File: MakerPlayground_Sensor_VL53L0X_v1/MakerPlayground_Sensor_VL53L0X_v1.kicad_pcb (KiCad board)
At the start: 2 copper layers, 30.4 x 19.9 mm, 18 parts, among them J1 Connector, Q1 BSS138, Q2 BSS138, U1 VL53L0X, U2 AP2127K-3.3

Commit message: Complete design.
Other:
- board text added: "v1.0"
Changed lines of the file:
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@@
   (general
     (thickness 1.6)
-    (drawings 223)
+    (drawings 224)
     (tracks 143)
     (zones 0)
@@
     (pad 1 np_thru_hole circle (at 0 0) (size 3 3) (drill 3) (layers *.Cu *.Mask))
   )
+  (gr_text v1.0 (at 143.75 114) (layer F.SilkS)
+    (effects (font (size 0.5 0.5) (thickness 0.1)))
+  )
   (gr_line (start 147.105 114.758) (end 147.177 114.714) (layer Edge.Cuts) (width 0.1))

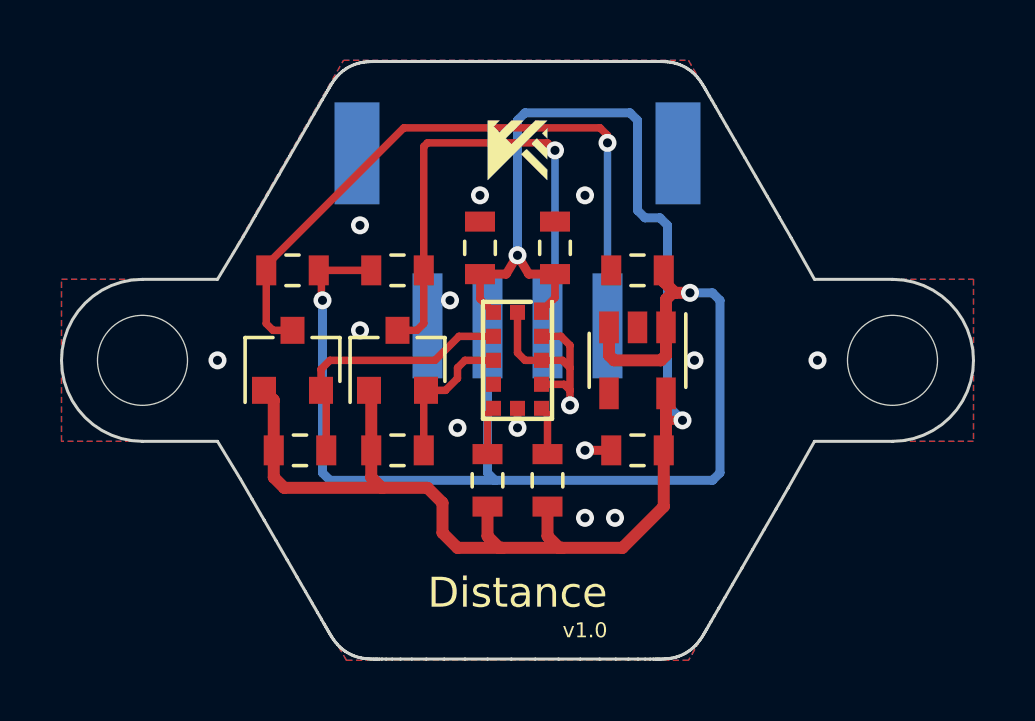
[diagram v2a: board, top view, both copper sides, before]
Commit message: Improve GND PTH, GND spreading area. Ready to fab.
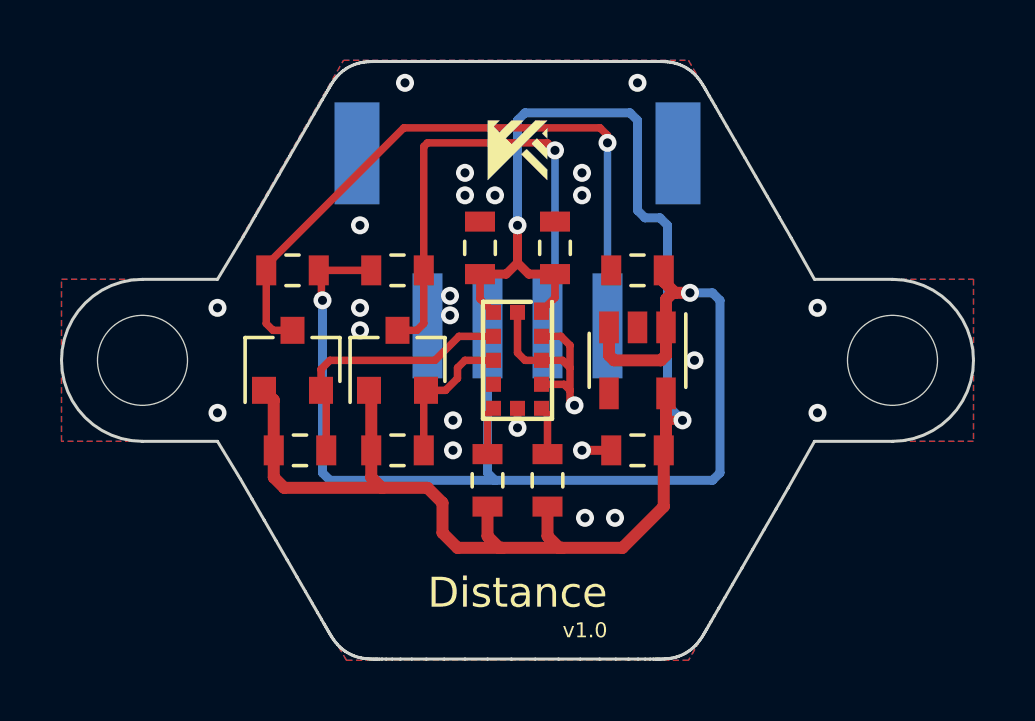
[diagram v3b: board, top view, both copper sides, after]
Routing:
- net GND: vias 14 -> 24
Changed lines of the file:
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@@
     (thickness 1.6)
     (drawings 224)
-    (tracks 143)
+    (tracks 154)
     (zones 0)
     (modules 18)
@@
     (44 Edge.Cuts user)
     (45 Margin user)
-    (46 B.CrtYd user)
-    (47 F.CrtYd user)
-    (48 B.Fab user)
-    (49 F.Fab user)
+    (46 B.CrtYd user hide)
+    (47 F.CrtYd user hide)
+    (48 B.Fab user hide)
+    (49 F.Fab user hide)
   )
   (setup
-    (last_trace_width 0.25)
+    (last_trace_width 0.3)
     (user_trace_width 0.15)
     (user_trace_width 0.2)
@@
     (fp_line (start -3.5 1.6) (end -3 0.892893) (layer B.Fab) (width 0.1))
     (fp_line (start -3 0.892893) (end -2.5 1.6) (layer B.Fab) (width 0.1))
-    (fp_text user %R (at 0 -1.5) (layer B.Fab)
+    (fp_text user %R (at 0 -1.5) (layer B.Fab) hide
       (effects (font (size 1 1) (thickness 0.15)) (justify mirror))
     )
@@
     (effects (font (size 1 1) (thickness 0.2)))
   )
-  (via (at 140.25 99.5) (size 0.6) (drill 0.3) (layers F.Cu B.Cu) (net 1))
-  (via (at 139.5 107.25) (size 0.6) (drill 0.3) (layers F.Cu B.Cu) (net 1))
-  (via (at 139.25 103) (size 0.6) (drill 0.3) (layers F.Cu B.Cu) (net 1))
+  (via (at 140.75 99.5) (size 0.6) (drill 0.3) (layers F.Cu B.Cu) (net 1))
+  (via (at 139.35 107) (size 0.6) (drill 0.3) (layers F.Cu B.Cu) (net 1))
+  (via (at 139.25 102.85) (size 0.6) (drill 0.3) (layers F.Cu B.Cu) (net 1))
   (segment (start 141.5 106.6) (end 141.5 107.25) (width 0.25) (layer F.Cu) (net 1))
   (via (at 141.5 107.25) (size 0.6) (drill 0.3) (layers F.Cu B.Cu) (net 1))
-  (via (at 143.75 108) (size 0.6) (drill 0.3) (layers F.Cu B.Cu) (net 1))
+  (via (at 143.65 108) (size 0.6) (drill 0.3) (layers F.Cu B.Cu) (net 1))
   (segment (start 144.5375 108) (end 143.75 108) (width 0.3) (layer F.Cu) (net 1) (status 10))
-  (via (at 131.5 105) (size 0.6) (drill 0.3) (layers F.Cu B.Cu) (net 1))
+  (via (at 131.5 106.75) (size 0.6) (drill 0.3) (layers F.Cu B.Cu) (net 1))
   (via (at 147.4 105) (size 0.6) (drill 0.3) (layers F.Cu B.Cu) (net 1))
   (segment (start 141.5 103.4) (end 141.5 104.75) (width 0.25) (layer F.Cu) (net 1))
   (segment (start 141.5 104.75) (end 141.75 105) (width 0.25) (layer F.Cu) (net 1))
   (segment (start 141.75 105) (end 142.3 105) (width 0.25) (layer F.Cu) (net 1))
-  (via (at 143.25 106.5) (size 0.6) (drill 0.3) (layers F.Cu B.Cu) (net 1))
+  (via (at 143.4 106.5) (size 0.6) (drill 0.3) (layers F.Cu B.Cu) (net 1))
   (segment (start 142.95 104.2) (end 143.25 104.5) (width 0.25) (layer F.Cu) (net 1))
   (segment (start 142.3 104.2) (end 142.95 104.2) (width 0.25) (layer F.Cu) (net 1))
@@
   (segment (start 143.25 105.25) (end 143.25 106) (width 0.25) (layer F.Cu) (net 1))
   (segment (start 143.25 106) (end 143.25 106.5) (width 0.25) (layer F.Cu) (net 1))
-  (via (at 143.75 99.5) (size 0.6) (drill 0.3) (layers F.Cu B.Cu) (net 1))
+  (via (at 143.65 99.5) (size 0.6) (drill 0.3) (layers F.Cu B.Cu) (net 1))
   (via (at 143.75 110.25) (size 0.6) (drill 0.3) (layers F.Cu B.Cu) (net 1))
   (via (at 144.75 110.25) (size 0.6) (drill 0.3) (layers F.Cu B.Cu) (net 1))
   (via (at 136.25 104) (size 0.6) (drill 0.3) (layers F.Cu B.Cu) (net 1))
   (via (at 136.25 100.5) (size 0.6) (drill 0.3) (layers F.Cu B.Cu) (net 1))
-  (via (at 151.5 105) (size 0.6) (drill 0.3) (layers F.Cu B.Cu) (net 1))
+  (via (at 137.75 95.75) (size 0.6) (drill 0.3) (layers F.Cu B.Cu) (net 1))
+  (via (at 145.5 95.75) (size 0.6) (drill 0.3) (layers F.Cu B.Cu) (net 1))
+  (via (at 131.5 103.25) (size 0.6) (drill 0.3) (layers F.Cu B.Cu) (net 1))
+  (via (at 151.5 103.25) (size 0.6) (drill 0.3) (layers F.Cu B.Cu) (net 1))
+  (via (at 151.5 106.75) (size 0.6) (drill 0.3) (layers F.Cu B.Cu) (net 1))
+  (via (at 139.35 108) (size 0.6) (drill 0.3) (layers F.Cu B.Cu) (net 1))
+  (via (at 139.75 99.5) (size 0.6) (drill 0.3) (layers F.Cu B.Cu) (net 1))
+  (via (at 139.25 103.5) (size 0.6) (drill 0.3) (layers F.Cu B.Cu) (net 1))
+  (via (at 136.25 103.25) (size 0.6) (drill 0.3) (layers F.Cu B.Cu) (net 1))
+  (via (at 139.75 98.75) (size 0.6) (drill 0.3) (layers F.Cu B.Cu) (net 1))
+  (via (at 143.65 98.75) (size 0.6) (drill 0.3) (layers F.Cu B.Cu) (net 1))
   (segment (start 144.55 103.9) (end 144.55 104.83) (width 0.4) (layer F.Cu) (net 2))
   (segment (start 144.55 104.83) (end 144.72 105) (width 0.4) (layer F.Cu) (net 2))
@@
   (segment (start 146.375 109.875) (end 145 111.25) (width 0.4) (layer F.Cu) (net 7))
   (segment (start 146.45 107.925) (end 146.375 108) (width 0.4) (layer F.Cu) (net 7))
-  (via (at 141.5 101.5) (size 0.6) (drill 0.3) (layers F.Cu B.Cu) (net 7))
   (segment (start 141.125 102.125) (end 140.25 102.125) (width 0.3) (layer F.Cu) (net 7))
-  (segment (start 141.5 101.5) (end 141.125 102.125) (width 0.3) (layer F.Cu) (net 7))
   (segment (start 141.875 102.125) (end 142.75 102.125) (width 0.3) (layer F.Cu) (net 7))
-  (segment (start 141.5 101.5) (end 141.875 102.125) (width 0.3) (layer F.Cu) (net 7))
+  (segment (start 146.25 100.25) (end 146.5 100.5) (width 0.3) (layer B.Cu) (net 7))
+  (segment (start 145.75 100.25) (end 146.25 100.25) (width 0.3) (layer B.Cu) (net 7))
+  (segment (start 145.5 100) (end 145.75 100.25) (width 0.3) (layer B.Cu) (net 7))
+  (segment (start 141.5 100.5) (end 141.5 97) (width 0.3) (layer B.Cu) (net 7))
+  (segment (start 145.25 96.75) (end 145.5 97) (width 0.3) (layer B.Cu) (net 7))
+  (via (at 141.5 100.5) (size 0.6) (drill 0.3) (layers F.Cu B.Cu) (net 7))
+  (segment (start 141.5 97) (end 141.75 96.75) (width 0.3) (layer B.Cu) (net 7))
+  (segment (start 141.75 96.75) (end 145.25 96.75) (width 0.3) (layer B.Cu) (net 7))
+  (segment (start 146.5 106.5) (end 147 107) (width 0.3) (layer B.Cu) (net 7))
   (segment (start 146.5 100.5) (end 146.5 106.5) (width 0.3) (layer B.Cu) (net 7))
-  (segment (start 141.5 97) (end 141.75 96.75) (width 0.3) (layer B.Cu) (net 7))
-  (segment (start 146.25 100.25) (end 146.5 100.5) (width 0.3) (layer B.Cu) (net 7))
-  (segment (start 141.5 101.5) (end 141.5 97) (width 0.3) (layer B.Cu) (net 7))
-  (segment (start 146.5 106.5) (end 147 107) (width 0.3) (layer B.Cu) (net 7))
-  (segment (start 141.75 96.75) (end 145.25 96.75) (width 0.3) (layer B.Cu) (net 7))
-  (segment (start 145.25 96.75) (end 145.5 97) (width 0.3) (layer B.Cu) (net 7))
-  (segment (start 145.75 100.25) (end 146.25 100.25) (width 0.3) (layer B.Cu) (net 7))
   (segment (start 145.5 97) (end 145.5 100) (width 0.3) (layer B.Cu) (net 7))
-  (segment (start 145.5 100) (end 145.75 100.25) (width 0.3) (layer B.Cu) (net 7))
+  (segment (start 141.125 102.125) (end 141.5 101.75) (width 0.3) (layer F.Cu) (net 7))
+  (segment (start 141.5 101.75) (end 141.875 102.125) (width 0.3) (layer F.Cu) (net 7))
+  (segment (start 141.5 101.75) (end 141.5 100.5) (width 0.3) (layer F.Cu) (net 7))
   (segment (start 140.5 108.125) (end 140.5 106.8) (width 0.25) (layer F.Cu) (net 8))
   (segment (start 140.5 106.8) (end 140.7 106.6) (width 0.25) (layer F.Cu) (net 8))
